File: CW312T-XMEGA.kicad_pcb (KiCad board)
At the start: 2 copper layers, 58.7 x 53.7 mm, 11 parts, among them P1 PCIEx4 EDGE CONNECTOR, U1 ATXMEGA128D4-AU

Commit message: updated schematic and pcb - Ready for review
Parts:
- moved R3 29.5 mm to (166.1, 101.0), turned to -90 degrees
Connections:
- net Net-(P1-FILT_LP) renamed /FILT_LP
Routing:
- net /CLK: track 50.0 -> 5.45 mm
- net Net-(P1-CLKIN): track 16.4 -> 58.6 mm
- net /PDID: track 85.5 -> 81.8 mm

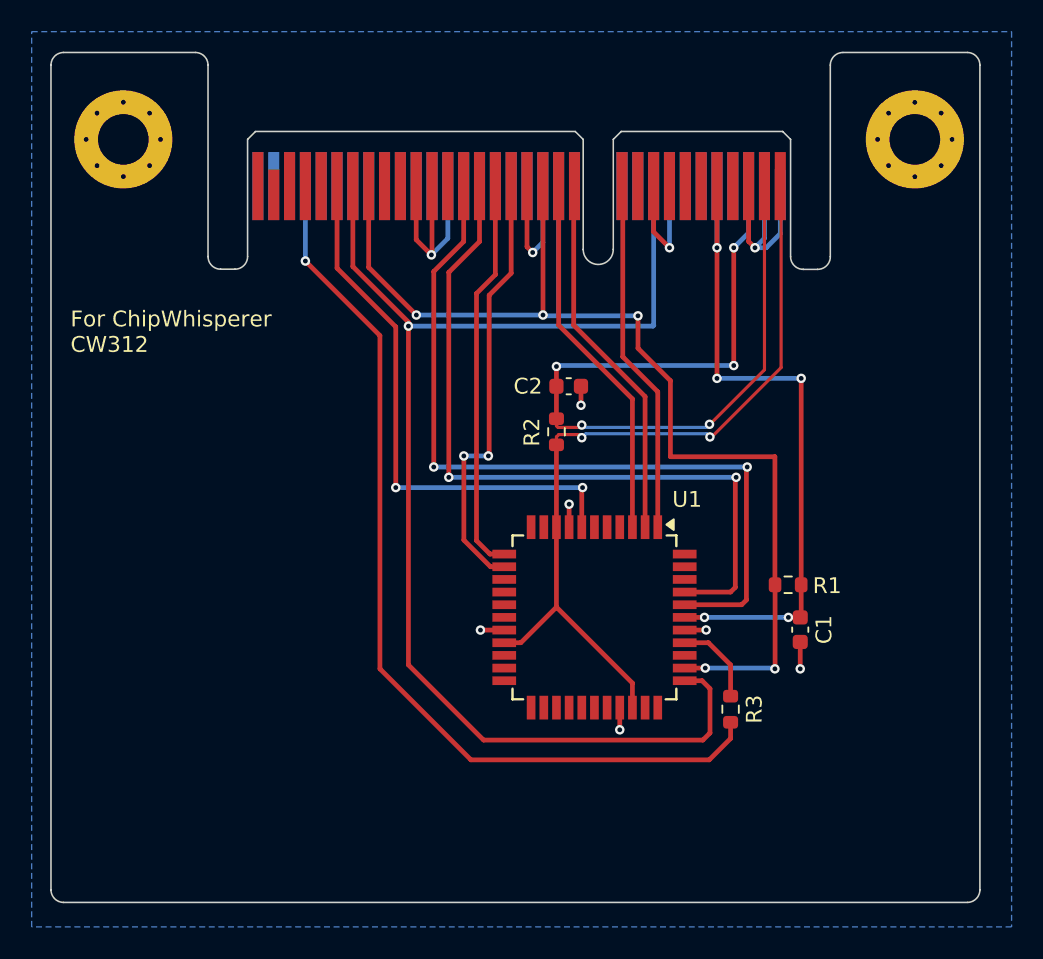
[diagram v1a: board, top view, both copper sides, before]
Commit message: updated power on schematic and routing, updated silkscreen
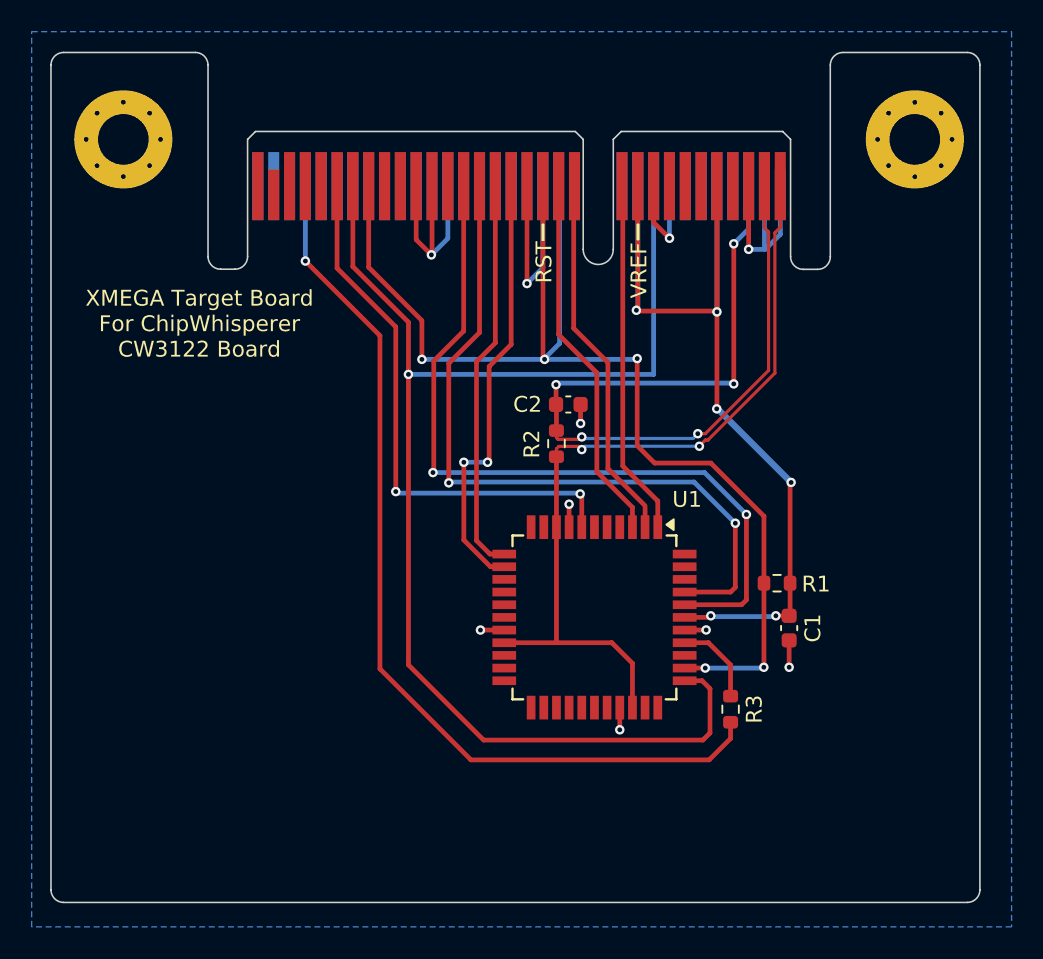
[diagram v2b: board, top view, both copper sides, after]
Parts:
- moved C2 1.15 mm to (155.8, 81.7)
- moved R2 0.75 mm to (155.1, 84.2)
- moved R1 0.71 mm to (169.0, 93.0)
- moved C1 0.71 mm to (169.8, 95.8)
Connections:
- P1 pad A10: unconnected-(P1-HDR2-PadA10) -> VCC
- P1 pad B10: unconnected-(P1-IOVREF-PadB10) -> VCC
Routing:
- net VCC: track 44.2 -> 64.8 mm, vias 5 -> 6
- net /HDR5/RST: track 75.4 -> 78.5 mm
- net /PDID: track 81.8 -> 84.9 mm
- net GND: track 52.1 -> 55.1 mm
- net /FILT_LP: track 53.1 -> 54.9 mm
- net /GPIO4: track 50.8 -> 49.2 mm
- net /GPIO3: track 47.6 -> 46.1 mm
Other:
- board text added: "RST"
- board text added: "VREF"
- board text added: "XMEGA Target Board For ChipWhisperer CW3122 Board"
- board text removed: "For ChipWhisperer CW312"

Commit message: updated schematic and pcb, after library reorganization
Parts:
- removed P1: PCIEx4 EDGE CONNECTOR, tutorial_2_library:CW312_Template
- added P2: PCIEx4 EDGE CONNECTOR, tutorial_2_library:CW312_Template, F.Cu at (127.7, 65.0)
